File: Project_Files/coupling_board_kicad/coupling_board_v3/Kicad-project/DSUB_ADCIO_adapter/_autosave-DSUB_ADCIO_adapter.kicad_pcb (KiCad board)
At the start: 2 copper layers, 36.1 x 70 mm, 6 parts, among them J1 Conn_02x04_Odd_Even, J10 Conn_02x12_Odd_Even, J2 Conn_02x04_Odd_Even, J3 Conn_02x04_Odd_Even, J5 Conn_02x12_Odd_Even, J6 DB25_Socket

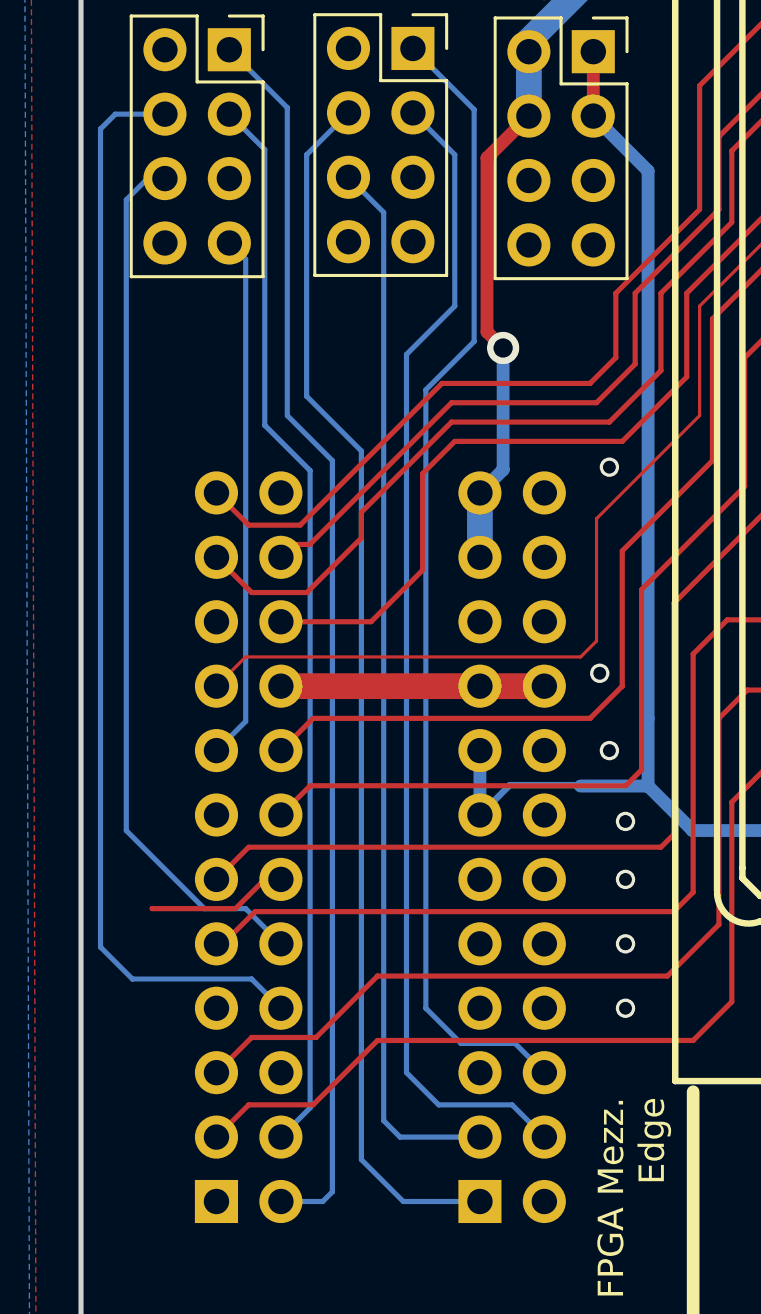
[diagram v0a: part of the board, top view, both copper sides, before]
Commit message: Fixed adcio coupler
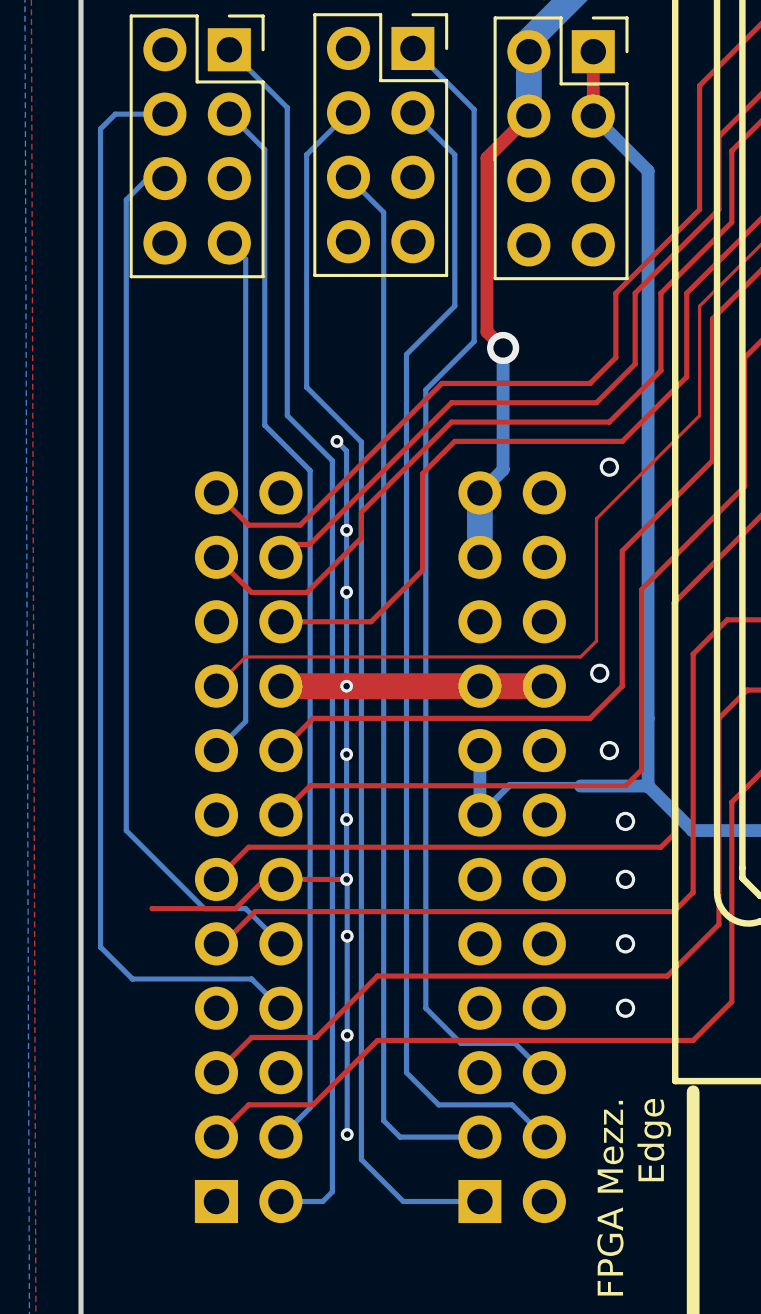
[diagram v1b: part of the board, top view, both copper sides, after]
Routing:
- net GND1: track 15.9 -> 46.0 mm, vias 7 -> 17
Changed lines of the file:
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@@
+	)
+	(segment
+		(start 135.6868 103.124)
+		(end 140.9446 103.124)
+		(width 1.016)
+		(layer "F.Cu")
+		(net 3)
 	)
 	(segment
@@
 	(segment
 		(start 133.096 103.124)
-		(end 140.9446 103.124)
+		(end 135.6868 103.124)
 		(width 1.016)
 		(layer "F.Cu")
@@
 		(start 132.461 110.744)
 		(end 131.3084 111.8966)
+		(width 0.2032)
+		(layer "F.Cu")
+		(net 3)
+	)
+	(segment
+		(start 135.6868 110.744)
+		(end 133.096 110.744)
 		(width 0.2032)
 		(layer "F.Cu")
@@
 	)
 	(via
+		(at 135.6868 105.8164)
+		(size 0.508)
+		(drill 0.254)
+		(layers "F.Cu" "B.Cu")
+		(free yes)
+		(net 3)
+	)
+	(via
 		(at 146.685 108.458)
 		(size 0.762)
@@
 	)
 	(via
+		(at 135.7122 116.8908)
+		(size 0.508)
+		(drill 0.254)
+		(layers "F.Cu" "B.Cu")
+		(free yes)
+		(net 3)
+	)
+	(via
 		(at 145.669 102.616)
 		(size 0.762)
@@
 	)
 	(via
+		(at 135.6868 99.4156)
+		(size 0.508)
+		(drill 0.254)
+		(layers "F.Cu" "B.Cu")
+		(net 3)
+	)
+	(via
+		(at 135.3058 93.472)
+		(size 0.508)
+		(drill 0.254)
+		(layers "F.Cu" "B.Cu")
+		(net 3)
+	)
+	(via
+		(at 135.6868 103.124)
+		(size 0.508)
+		(drill 0.254)
+		(layers "F.Cu" "B.Cu")
+		(net 3)
+	)
+	(via
+		(at 135.6868 108.3818)
+		(size 0.508)
+		(drill 0.254)
+		(layers "F.Cu" "B.Cu")
+		(free yes)
+		(net 3)
+	)
+	(via
+		(at 135.6868 96.9772)
+		(size 0.508)
+		(drill 0.254)
+		(layers "F.Cu" "B.Cu")
+		(free yes)
+		(net 3)
+	)
+	(via
+		(at 135.7122 120.8024)
+		(size 0.508)
+		(drill 0.254)
+		(layers "F.Cu" "B.Cu")
+		(free yes)
+		(net 3)
+	)
+	(via
 		(at 146.685 113.284)
 		(size 0.762)
@@
 	)
 	(via
+		(at 135.6868 110.744)
+		(size 0.508)
+		(drill 0.254)
+		(layers "F.Cu" "B.Cu")
+		(free yes)
+		(net 3)
+	)
+	(via
 		(at 146.05 94.488)
 		(size 0.762)
@@
 		(net 3)
 	)
+	(via
+		(at 135.7122 112.9792)
+		(size 0.508)
+		(drill 0.254)
+		(layers "F.Cu" "B.Cu")
+		(free yes)
+		(net 3)
+	)
+	(segment
+		(start 135.6868 110.744)
+		(end 135.6868 108.3818)
+		(width 0.2032)
+		(layer "B.Cu")
+		(net 3)
+	)
+	(segment
+		(start 135.7122 116.8908)
+		(end 135.7122 112.9792)
+		(width 0.2032)
+		(layer "B.Cu")
+		(net 3)
+	)
+	(segment
+		(start 135.6868 96.9772)
+		(end 135.6868 93.853)
+		(width 0.2032)
+		(layer "B.Cu")
+		(net 3)
+	)
+	(segment
+		(start 135.6868 99.4156)
+		(end 135.6868 103.124)
+		(width 0.2032)
+		(layer "B.Cu")
+		(net 3)
+	)
+	(segment
+		(start 135.7122 116.8908)
+		(end 135.7122 120.8024)
+		(width 0.2032)
+		(layer "B.Cu")
+		(net 3)
+	)
+	(segment
+		(start 135.6868 105.8164)
+		(end 135.6868 103.124)
+		(width 0.2032)
+		(layer "B.Cu")
+		(net 3)
+	)
+	(segment
+		(start 135.7122 110.7694)
+		(end 135.6868 110.744)
+		(width 0.2032)
+		(layer "B.Cu")
+		(net 3)
+	)
+	(segment
+		(start 135.6868 105.8164)
+		(end 135.6868 108.3818)
+		(width 0.2032)
+		(layer "B.Cu")
+		(net 3)
+	)
+	(segment
+		(start 135.6868 93.853)
+		(end 135.3058 93.472)
+		(width 0.2032)
+		(layer "B.Cu")
+		(net 3)
+	)
+	(segment
+		(start 135.7122 112.9792)
+		(end 135.7122 110.7694)
+		(width 0.2032)
+		(layer "B.Cu")
+		(net 3)
+	)
+	(segment
+		(start 135.6868 99.4156)
+		(end 135.6868 96.9772)
+		(width 0.2032)
+		(layer "B.Cu")
+		(net 3)
+	)
 	(segment
 		(start 153.4744 100.5078)
@@
 	)
 	(segment
+		(start 137.922 123.444)
+		(end 140.9446 123.444)
+		(width 0.2032)
+		(layer "B.Cu")
+		(net 36)
+	)
+	(segment
+		(start 136.271 93.4974)
+		(end 136.271 121.793)
+		(width 0.2032)
+		(layer "B.Cu")
+		(net 36)
+	)
+	(segment
+		(start 134.112 82.169)
+		(end 134.112 91.3384)
+		(width 0.2032)
+		(layer "B.Cu")
+		(net 36)
+	)
+	(segment
 		(start 136.271 121.793)
 		(end 137.922 123.444)
@@
 	)
 	(segment
-		(start 136.271 93.853)
-		(end 136.271 121.793)
-		(width 0.2032)
-		(layer "B.Cu")
-		(net 36)
-	)
-	(segment
-		(start 134.112 91.694)
-		(end 136.271 93.853)
-		(width 0.2032)
-		(layer "B.Cu")
-		(net 36)
-	)
-	(segment
-		(start 137.922 123.444)
-		(end 140.9446 123.444)
-		(width 0.2032)
-		(layer "B.Cu")
-		(net 36)
-	)
-	(segment
-		(start 134.112 82.169)
-		(end 134.112 91.694)
-		(width 0.2032)
-		(layer "B.Cu")
+		(start 134.112 91.3384)
+		(end 136.271 93.4974)
+		(width 0.2032)
+		(layer "B.Cu")
